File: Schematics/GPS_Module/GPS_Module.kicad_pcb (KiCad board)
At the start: 4 copper layers, 69.5 x 60 mm, 66 parts, among them J1 Stack Male Edge Connector, J2 SWD_01x04_Pin, J3 25SH-B-06-TR, J6 USB_B_Micro, Q1 AO3400A, SW1 SW_STM_RESET, SW2 SW_STM_BOOT_MODE, U1 STM32F103CBTx, U10 AMS1117-3.3, U3 W25Q128JVS, U4 LM66100DCKR, U5 LM66100DCKR, U6 LM66100DCKR, U7 ACS70331EOLC, U9 ISO1042BQDWVR, Y1 X322516MMB4SI

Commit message: preliminary PCB design
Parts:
- removed C19: 1uF, Capacitor_SMD:CP_Elec_4x5.4
- removed J3: 25SH-B-06-TR, Connector_PinHeader_2.54mm:PinHeader_1x06_P2.54mm_Horizontal
- added C12: 1uF, Capacitor_SMD:C_0805_2012Metric, F.Cu at (49.6, 43.0)
- added D1: PPS_LED (YLW), LED_SMD:LED_0603_1608Metric, F.Cu at (121.2, 65.9)
- added J4: Stack Male Edge Connector, Connector_PCBEdge:BUS_PCIexpress_x1, F.Cu at (66.4, 21.0)
- added R1: 560R, Resistor_SMD:R_0603_1608Metric, F.Cu at (106.4, 73.3)
- C10: value 10u -> 10uF
- C18: footprint Capacitor_SMD:CP_Elec_4x5.4 -> Capacitor_SMD:C_0805_2012Metric
- D9: moved to B.Cu
- J1: value Stack Male Edge Connector -> 470804001; footprint Connector_PCBEdge:BUS_PCIexpress_x1 -> footprints:CONN_47080-4001_MOL_SATA; moved to B.Cu
- SW1, SW2: footprint PTS636:PTS636_SK43_SMTR_LFS -> Button_Switch_SMD:SW_Push_1P1T_XKB_TS-1187A
- U4, U5, U6: footprint LMR66100:SC-70-6 -> LMR66100:SC-70-6_Handsoldering
- moved J1 66.9 mm to (58.3, 87.4)
- moved SW2 8.09 mm to (76.4, 55.3), turned to 180 degrees
- moved Q1 6.65 mm to (63.8, 41.4)
- moved R9 6.50 mm to (63.9, 44.2)
- moved C5 6.43 mm to (36.3, 42.5)
- moved C1 6.40 mm to (33.1, 31.6)
- moved D8 6.21 mm to (70.0, 59.7)
- moved C16 6.10 mm to (58.2, 60.8)
- moved C4 6.10 mm to (37.7, 62.7)
- moved U3 6.10 mm to (46.4, 60.3)
- moved BZ1 6.10 mm to (69.0, 43.6)
- moved C11 6.10 mm to (49.8, 57.3)
- moved C13 6.10 mm to (42.7, 60.2)
- moved C14 6.10 mm to (58.9, 48.2)
- moved C15 6.10 mm to (61.5, 52.0)
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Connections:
- C18 pad 1: +3.3VA -> +3.3V
- D10 pad 2: V_BATT -> +BATT
- R11 pad 2: Net-(Q1-G) -> BUZZER
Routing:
- net DB_LED: track 96.8 -> 8.48 mm, vias 1 -> 0
- net V_PSU: track 47.4 -> 4.41 mm, vias 3 -> 0
- net GND: track 148.5 -> 112.7 mm, vias 30 -> 29
- net V_BATT: track 26.6 -> 0.00 mm
- net +5V: track 33.0 -> 10.9 mm, vias 1 -> 0
- net CAN_H: track 17.1 -> 2.10 mm
- net +3.3V: track 215.5 -> 200.6 mm, vias 16 -> 17
- net CAN_L: track 15.9 -> 1.39 mm
- net SDA_GPS: track 25.9 -> 14.3 mm
- net SCL_GPS: track 23.9 -> 13.7 mm
- net EXTINT_GPS: track 23.7 -> 16.5 mm
- net BOOT0: track 16.3 -> 23.3 mm
- net SWDIO: track 19.6 -> 25.9 mm
- net SWCLK: track 8.51 -> 14.6 mm
- net USB_D+: track 10.9 -> 17.0 mm
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
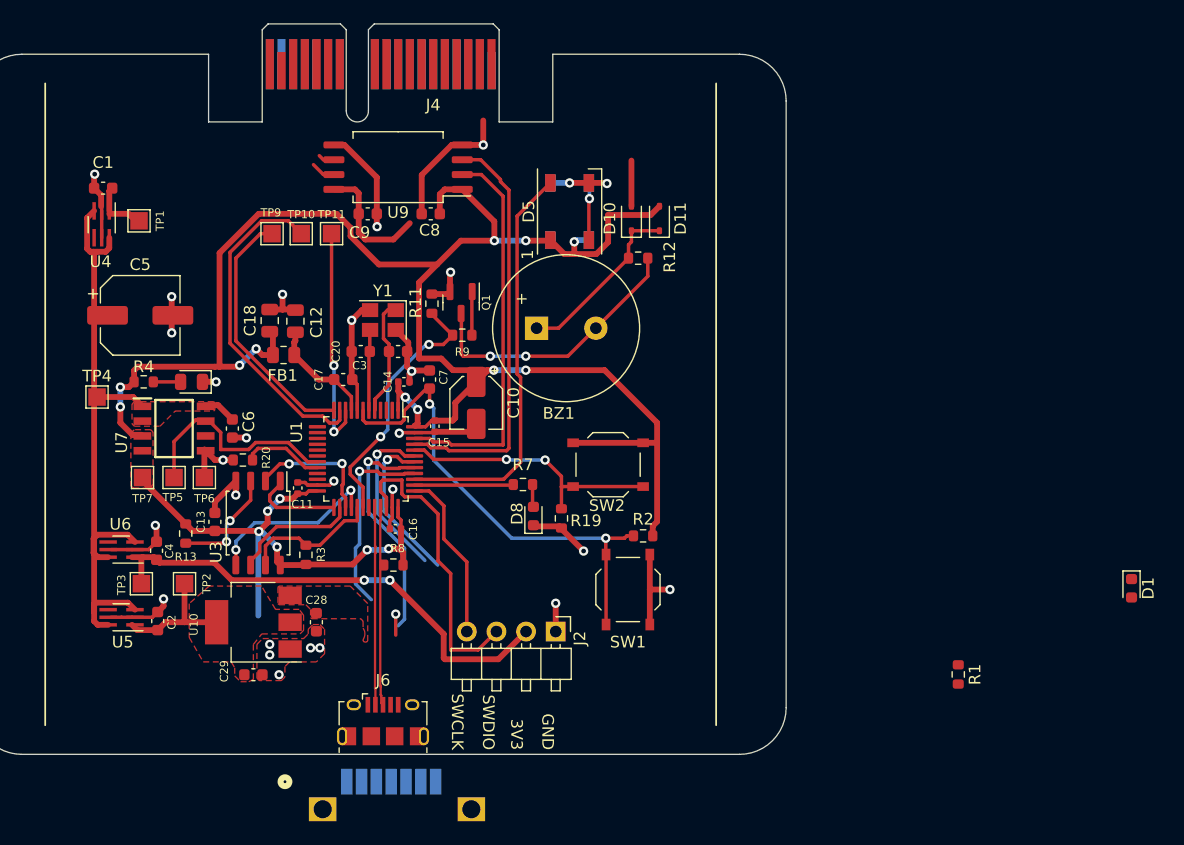
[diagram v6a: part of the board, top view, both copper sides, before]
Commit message: finished gps module updates waiting for approval
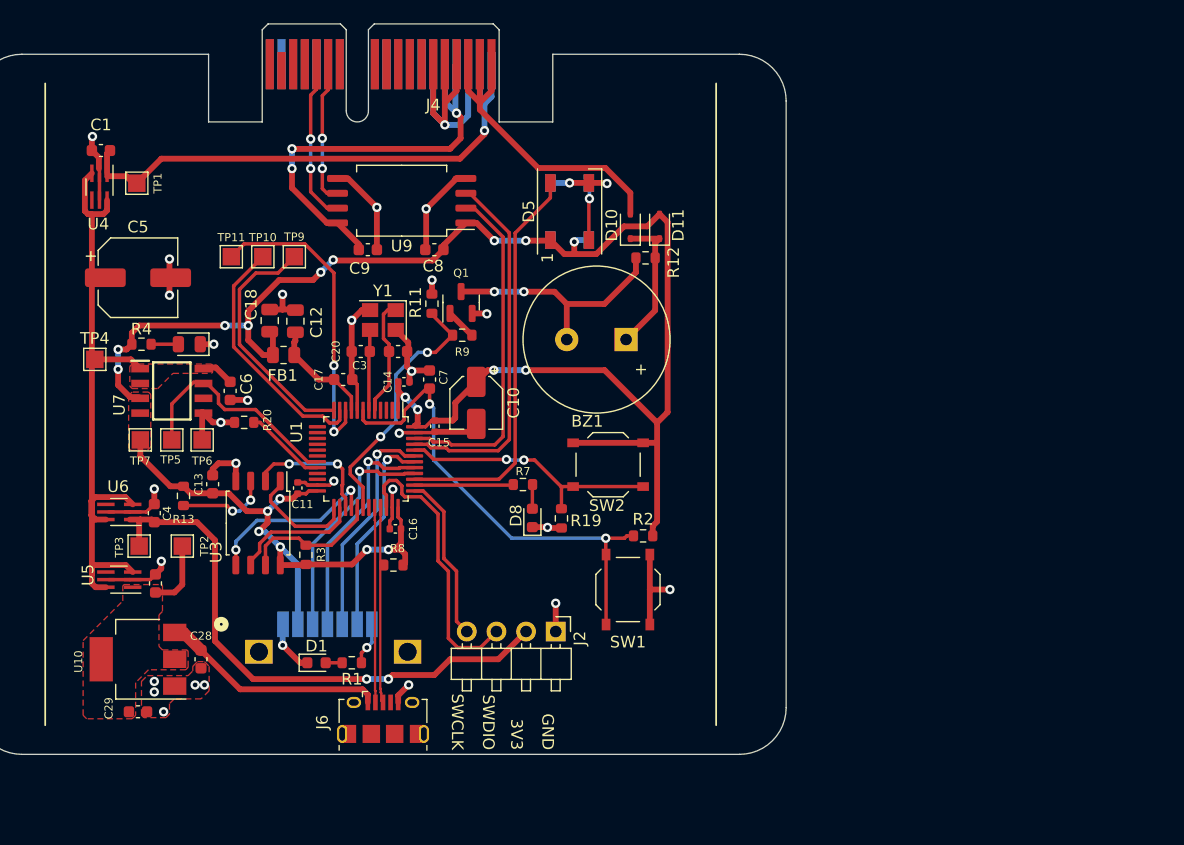
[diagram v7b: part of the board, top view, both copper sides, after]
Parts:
- moved D1 70.1 mm to (51.4, 72.3), turned to 0 degrees
- moved R1 52.0 mm to (54.4, 72.3), turned to 0 degrees
- moved J1 14.6 mm to (52.8, 73.9)
- moved C28 10.4 mm to (41.5, 72.0)
- moved C29 10.4 mm to (36.1, 76.5)
- moved U10 10.4 mm to (36.1, 72.0)
- moved BZ1 10.3 mm to (79.2, 44.6), turned to 180 degrees
- moved TP11 8.82 mm to (44.1, 37.5)
- moved TP10 3.84 mm to (46.8, 37.5)
- moved C5 3.23 mm to (36.1, 39.3)
- moved TP4 3.23 mm to (32.4, 46.3)
- moved C1 3.23 mm to (32.9, 28.4)
- moved TP1 3.23 mm to (36.0, 31.2)
- moved C13 3.23 mm to (42.5, 57.0)
- moved C2 3.23 mm to (37.6, 65.5)
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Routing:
- net V_PSU: track 4.41 -> 45.2 mm, vias 0 -> 1
- net +5V: track 10.9 -> 37.6 mm, vias 0 -> 3
- net +BATT: track 3.91 -> 29.0 mm
- net GND: track 112.7 -> 136.1 mm, vias 29 -> 32
- net /USB_5V: track 0.00 -> 19.4 mm
- net +3.3V: track 200.6 -> 185.2 mm, vias 17 -> 19
- net CAN_H: track 2.10 -> 14.0 mm, vias 0 -> 2
- net CAN_L: track 1.39 -> 12.3 mm, vias 0 -> 2
- net Net-(U1-PA1): track 28.6 -> 21.5 mm
- net V_SWD: track 41.8 -> 48.6 mm
- net Net-(U1-PA0): track 19.7 -> 26.3 mm
- net V_REGUSB: track 12.3 -> 5.98 mm
- net SDA_GPS: track 14.3 -> 19.3 mm
- net SCL_GPS: track 13.7 -> 17.8 mm
- net CAN_RX: track 35.7 -> 31.6 mm
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- removed copper zone on F.Cu, net /USB_5V

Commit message: starting daughter board PCB layout
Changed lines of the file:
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@@
   (segment (start 56.391352 50.663) (end 56.391352 49.7255) (width 0.3) (layer "F.Cu") (net 11))
   (segment (start 57.565852 73.7) (end 57.915852 73.35) (width 0.5) (layer "F.Cu") (net 12))
-  (segment (start 42.7 61.8) (end 42.7 70.436111) (width 0.5) (layer "F.Cu") (net 12))
   (segment (start 35.4 60.025) (end 36.3 60.025) (width 0.5) (layer "F.Cu") (net 12))
-  (segment (start 45.963889 73.7) (end 55.7 73.7) (width 0.5) (layer "F.Cu") (net 12))
   (segment (start 36.2 60.125) (end 36.3 60.025) (width 0.5) (layer "F.Cu") (net 12))
   (segment (start 37.275 60.025) (end 37.5 60.25) (width 0.5) (layer "F.Cu") (net 12))
+  (segment (start 42.7 70.9) (end 45.5 73.7) (width 0.5) (layer "F.Cu") (net 12))
   (segment (start 61.501472 73.35) (end 62.851472 72) (width 0.5) (layer "F.Cu") (net 12))
-  (segment (start 42.7 70.436111) (end 45.963889 73.7) (width 0.5) (layer "F.Cu") (net 12))
+  (segment (start 37.5 60.25) (end 41.15 60.25) (width 0.5) (layer "F.Cu") (net 12))
   (segment (start 36.2 62.2) (end 36.2 60.125) (width 0.5) (layer "F.Cu") (net 12))
   (segment (start 57.915852 73.35) (end 61.501472 73.35) (width 0.5) (layer "F.Cu") (net 12))
-  (segment (start 42.7 61.8) (end 41.15 60.25) (width 0.5) (layer "F.Cu") (net 12))
   (segment (start 66.985 72) (end 69.36 69.625) (width 0.5) (layer "F.Cu") (net 12))
+  (segment (start 41.15 60.25) (end 42.7 61.8) (width 0.5) (layer "F.Cu") (net 12))
+  (segment (start 42.7 61.8) (end 42.7 70.9) (width 0.5) (layer "F.Cu") (net 12))
   (segment (start 66.985 72) (end 62.851472 72) (width 0.5) (layer "F.Cu") (net 12))
-  (segment (start 41.15 60.25) (end 37.5 60.25) (width 0.5) (layer "F.Cu") (net 12))
   (segment (start 36.3 60.025) (end 37.275 60.025) (width 0.5) (layer "F.Cu") (net 12))
+  (segment (start 45.5 73.7) (end 55.7 73.7) (width 0.5) (layer "F.Cu") (net 12))
   (via (at 55.7 73.7) (size 0.8) (drill 0.4) (layers "F.Cu" "B.Cu") (net 12))
   (via (at 57.565852 73.7) (size 0.8) (drill 0.4) (layers "F.Cu" "B.Cu") (net 12))
